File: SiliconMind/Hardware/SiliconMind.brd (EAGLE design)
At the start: 100 x 80 mm, 38 parts, among them IC1 LM358, Q1 20MHz, U1 328P, U2 MCP4921PDIP, U3 7805, U4 QUAD_OPAMP

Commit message: added micro match connector
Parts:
- added X1: MICROMATCH-20, con-amp-micromatch:MICROMATCH-20
- moved D1 18.0 mm to (31.8, 49.5)
- moved D2 18.0 mm to (31.8, 39.4)
- moved D3 18.0 mm to (31.8, 54.6)
- moved R19 18.0 mm to (33.0, 26.7)
- moved R15 18.0 mm to (33.0, 21.6)
- moved C6 18.0 mm to (31.8, 33.0)
- moved R18 18.0 mm to (31.8, 44.5)
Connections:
- net TRIG renamed N$17
- removed net B_TRIG: U1.5
- removed net SCL: U1.28
- removed net SDA: U1.27
- removed net T8: U1.13
- new net T0: U1.23
- net T1: now also U1.24; no longer U1.11
- net T2: now also U1.25; no longer U1.6
- net T3: now also U1.26; no longer U1.25
- net T4: now also U1.27; no longer U1.26
- net T5: now also U1.28; no longer U1.23
- net T6: now also U1.2; no longer U1.24
- net T7: now also U1.3; no longer U1.12

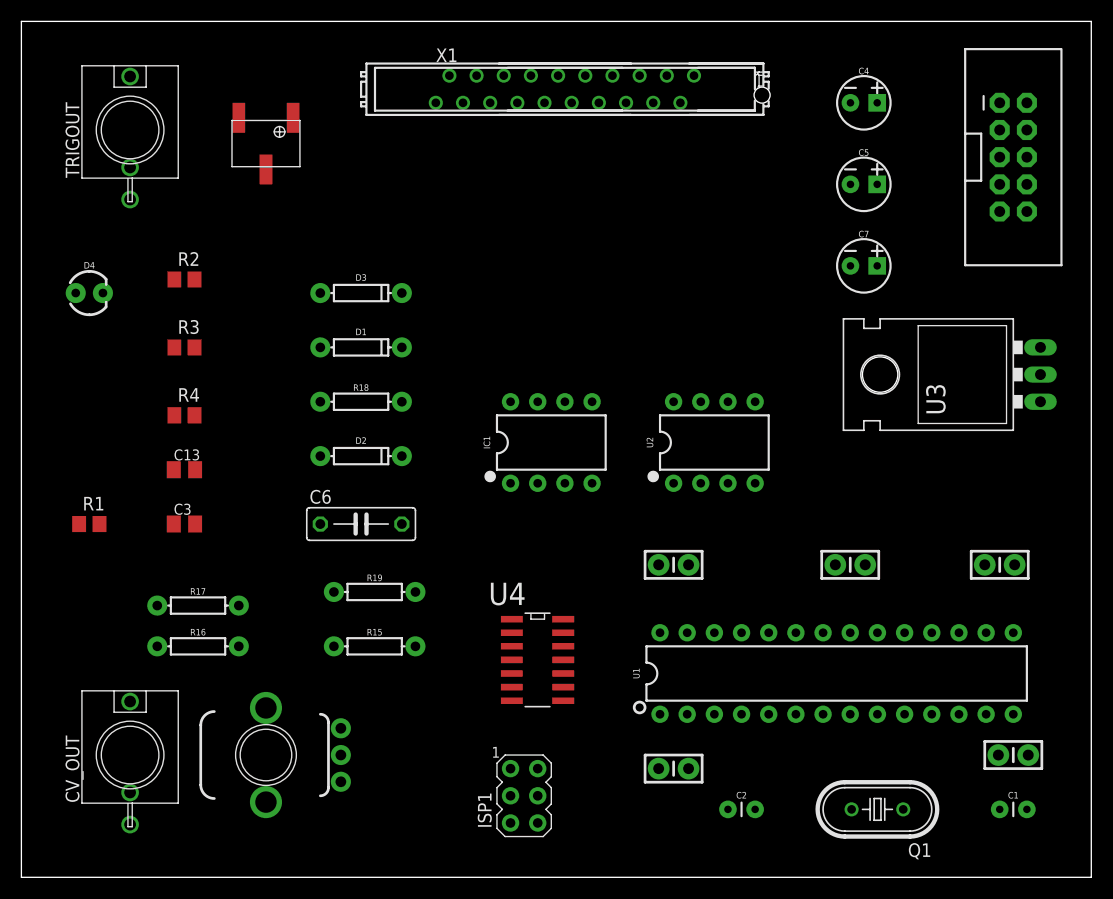
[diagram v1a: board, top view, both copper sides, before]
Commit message: Changed TL074 to TTL
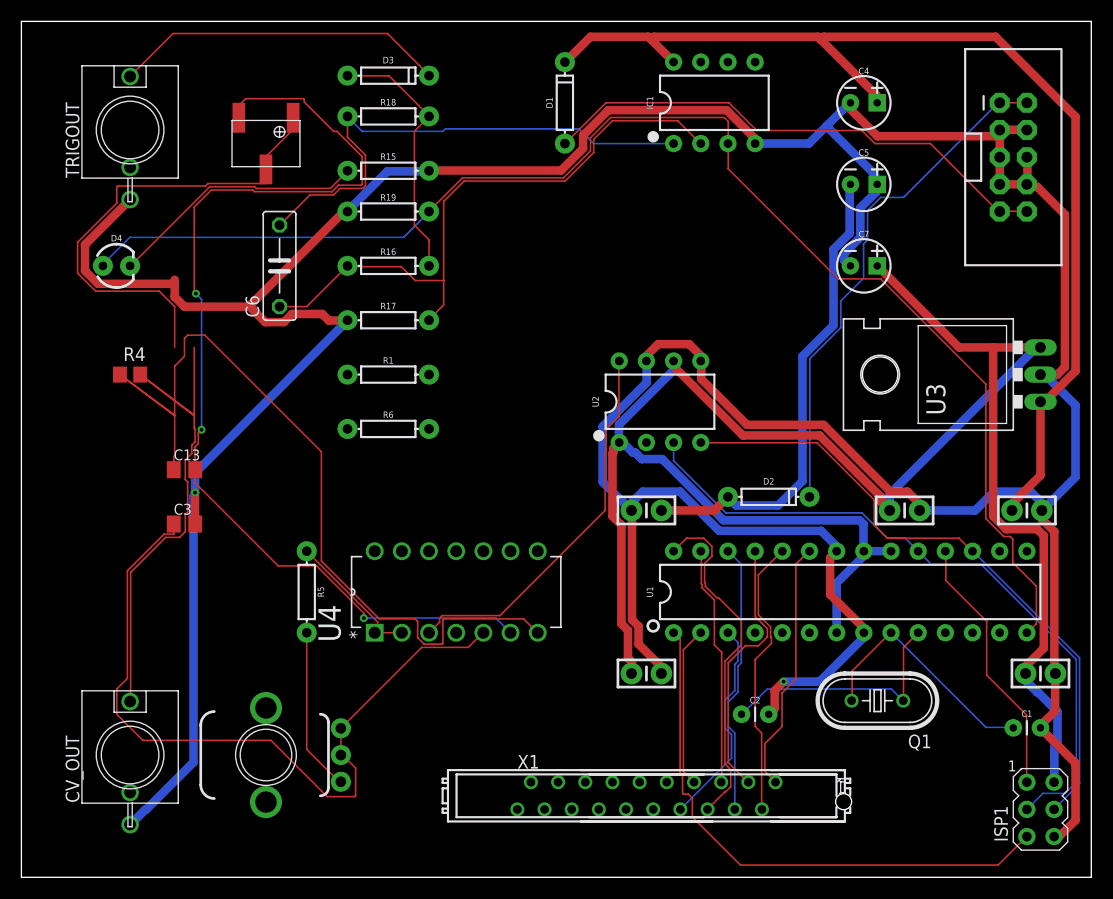
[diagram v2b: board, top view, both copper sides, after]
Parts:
- removed R2: 10K, rcl:R0805
- removed R3: 10k, rcl:R0805
- added R5: 200R, SparkFun-Resistors:AXIAL-0.3
- added R6: 10K, SparkFun-Resistors:AXIAL-0.3
- R1: value 200R -> 10K; device rcl:R0805 -> SparkFun-Resistors:AXIAL-0.3
- U4: value QUAD_OPAMP -> (none); device INSTRUO:QUAD_OPAMP -> INSTRUO:DIP254P762X533-14
- moved X1 66.5 mm to (58.4, 7.62)
- moved ISP1 48.3 mm to (95.2, 6.35)
- moved R15 44.5 mm to (34.3, 66.0)
- moved R16 39.8 mm to (34.3, 57.1)
- moved D2 38.3 mm to (69.8, 35.6)
- moved R19 35.6 mm to (34.3, 62.2)
- moved IC1 35.2 mm to (64.8, 72.4)
- moved R17 32.1 mm to (34.3, 52.1)
- moved R1 31.2 mm to (34.3, 47.0)
- moved D1 29.8 mm to (50.8, 72.4), turned to 90 degrees
- moved R18 26.8 mm to (34.3, 71.1)
- moved C6 25.3 mm to (24.1, 57.1), turned to 90 degrees
- moved D3 20.5 mm to (34.3, 74.9)
- moved Q1 10.2 mm to (80.0, 16.5)
- moved U4 10.2 mm to (48.3, 30.5), turned to 90 degrees
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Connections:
- net GND: now also R1.P$1; no longer R2.1
- net N$11: now also U4.7; no longer U4.2OUT
- net N$12: now also R1.P$2, U4.6; no longer R2.2, U4.2-IN
- net N$3: now also U4.3; no longer U4.1+IN
- net N$4: now also R5.P$1, U4.1, U4.2; no longer R1.1, U4.1-IN, U4.1OUT
- net N$5: now also R5.P$2; no longer R1.2
- net N$6: now also U4.5; no longer U4.2+IN
- net N$7: now also R6.P$1; no longer R3.1
- net N$8: now also R6.P$2; no longer R3.2
- net T0: now also X1.1
- net T1: now also X1.2
- net T2: now also X1.3
- net T3: now also X1.4
- net T4: now also X1.5
- net T5: now also X1.6
- net T6: now also X1.7
- net T7: now also X1.8
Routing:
- net GND: track 0.00 -> 405.6 mm, vias 0 -> 2
- net +5V: track 0.00 -> 184.8 mm
- net TRIGO: track 0.00 -> 128.0 mm
- net +12V: track 0.00 -> 102.8 mm
- net N$12: track 0.00 -> 96.4 mm, vias 0 -> 3
- net N$11: track 0.00 -> 80.2 mm
- net N$6: track 0.00 -> 70.1 mm
- net SCK: track 0.00 -> 64.2 mm
- net MOSI: track 0.00 -> 60.3 mm
- net N$32: track 0.00 -> 58.0 mm
- net RST: track 0.00 -> 52.4 mm
- net N$8: track 0.00 -> 49.2 mm
- net N$9: track 0.00 -> 49.0 mm
- net N$33: track 0.00 -> 48.5 mm
- net N$10: track 0.00 -> 48.1 mm
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
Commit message: added IDC connector
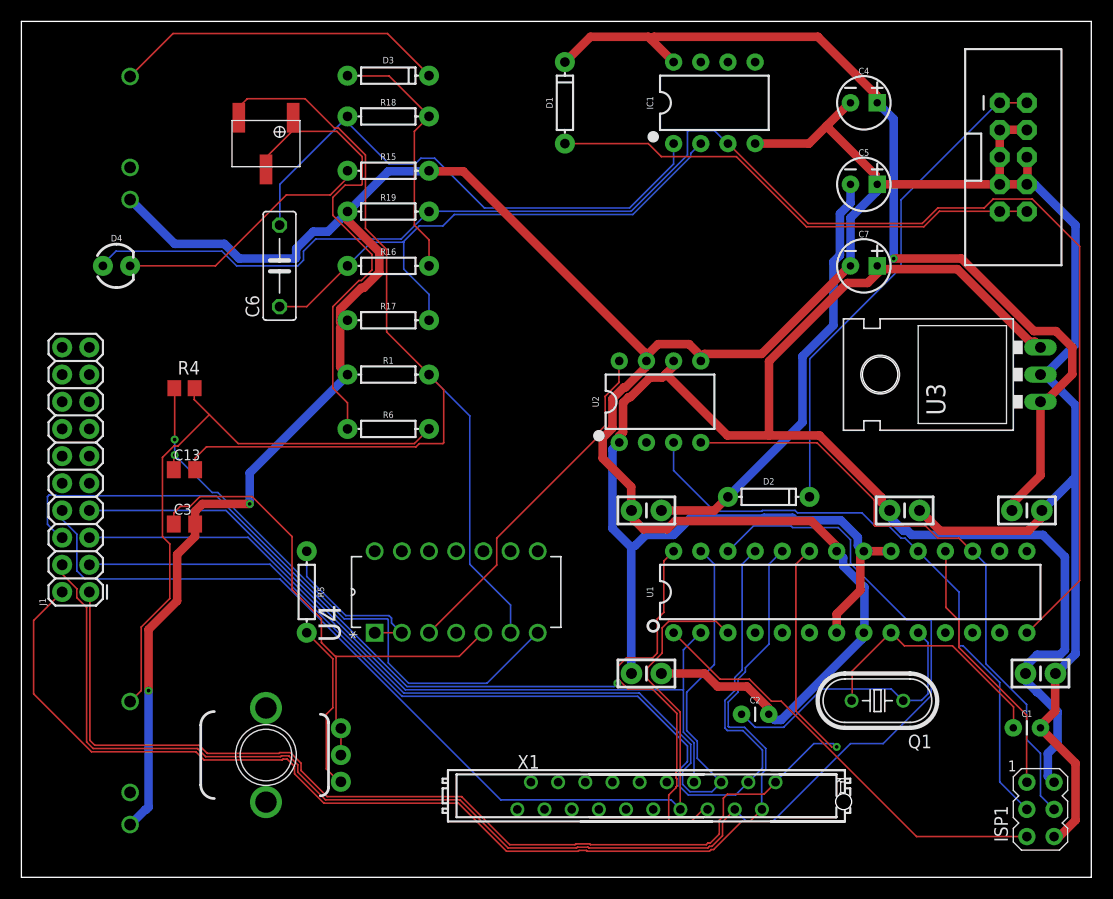
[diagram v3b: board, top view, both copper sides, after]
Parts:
- added J1: (no value), SparkFun-Connectors:2X10
- moved R4 5.24 mm to (15.2, 45.7)
- flipped CV_OUT to the bottom
- flipped TRIGOUT to the bottom
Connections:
- net T0: now also J1.1
- net T1: now also J1.2
- net T2: now also J1.3
- net T3: now also J1.4
- net T4: now also J1.5
- net T5: now also J1.6
- net T6: now also J1.7
- net T7: now also J1.8
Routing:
- net T3: track 25.4 -> 140.6 mm
- net T0: track 23.8 -> 114.8 mm, vias 0 -> 1
- net T1: track 26.5 -> 115.6 mm
- net T7: track 19.6 -> 97.5 mm
- net T2: track 25.1 -> 99.9 mm
- net T4: track 22.5 -> 97.1 mm
- net T5: track 32.6 -> 102.5 mm, vias 0 -> 1
- net T6: track 15.1 -> 77.5 mm
- net GND: track 405.6 -> 370.2 mm
- net N$11: track 80.2 -> 54.8 mm, vias 0 -> 2
- net N$6: track 70.1 -> 51.4 mm
- net TRIGO: track 128.0 -> 144.1 mm
- net +12V: track 102.8 -> 89.4 mm, vias 0 -> 1
- net RST: track 52.4 -> 40.9 mm
- net SCK: track 64.2 -> 57.2 mm
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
